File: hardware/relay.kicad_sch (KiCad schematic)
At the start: 5 parts, among them K1 SRD-05VDC-SL-C, Q1 BC847

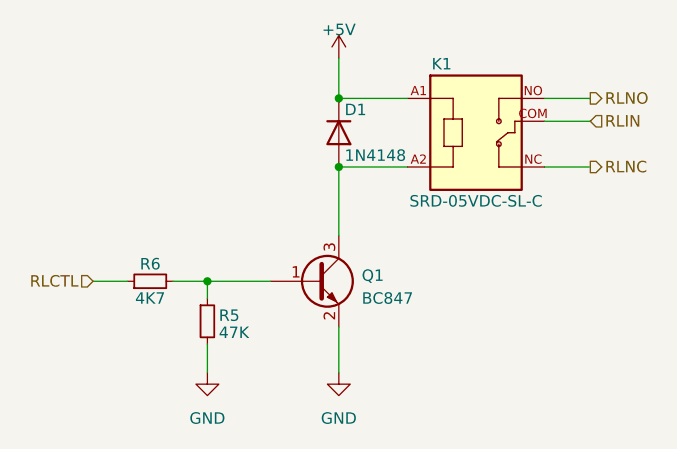
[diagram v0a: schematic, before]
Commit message: * 3V8 Power design fixed * Footprints assigned * Bom exported * PCB filter module placed
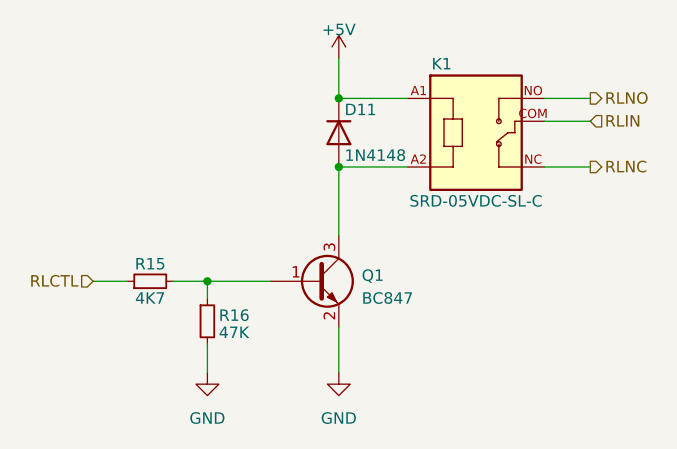
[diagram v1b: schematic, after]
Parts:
- R15: renamed from R6; footprint (none) -> Resistor_SMD:R_0603_1608Metric
- R16: renamed from R5; footprint (none) -> Resistor_SMD:R_0603_1608Metric
- renumbered D1 to D11
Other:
- company: (none) -> Hidro Elektronik
- title: (none) -> 2023 Staj Projesi
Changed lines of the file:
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@@
 (kicad_sch (version 20230121) (generator eeschema)
   (paper "A4")
+  (title_block
+    (title "2023 Staj Projesi")
+    (date "2023-07-24")
+    (rev "1.0")
+    (company "Hidro Elektronik")
+    (comment 1 "Mehmet Emre SAYGI(2019513057@ogr.cu.edu.tr)")
+    (comment 2 "Yilmaz Can DURAN(duranyilmazcan@gmail.com)")
+    (comment 3 "Asli VEZIR(vezirasli@gmail.com)")
+  )
   (junction (at 137.16 88.265) (diameter 0) (color 0 0 0 0)
   )
@@
   (symbol (lib_id "power:GND") (at 137.16 111.125 0) (unit 1)
     (in_bom yes) (on_board yes) (dnp no) (fields_autoplaced)
-    (property "Reference" "#PWR02" (at 137.16 117.475 0)
+    (property "Reference" "#PWR045" (at 137.16 117.475 0)
       (effects (font (size 1.27 1.27)) hide)
     )
@@
       (project "2023-staj-projesi"
         (path "/069db7ad-35cd-4aa8-8111-e026f632a4df/9708c89c-3f17-4bed-9aa3-84d886db37e6"
-          (reference "#PWR02") (unit 1)
+          (reference "#PWR045") (unit 1)
         )
       )
@@
   (symbol (lib_id "Diode:1N4148") (at 137.16 84.455 270) (unit 1)
     (in_bom yes) (on_board yes) (dnp no)
-    (property "Reference" "D1" (at 137.795 81.915 90)
+    (property "Reference" "D11" (at 137.795 81.915 90)
       (effects (font (size 1.27 1.27)) (justify left))
     )
@@
       (project "2023-staj-projesi"
         (path "/069db7ad-35cd-4aa8-8111-e026f632a4df/9708c89c-3f17-4bed-9aa3-84d886db37e6"
-          (reference "D1") (unit 1)
+          (reference "D11") (unit 1)
         )
       )
@@
   (symbol (lib_id "power:+5V") (at 137.16 76.2 0) (unit 1)
     (in_bom yes) (on_board yes) (dnp no) (fields_autoplaced)
-    (property "Reference" "#PWR01" (at 137.16 80.01 0)
+    (property "Reference" "#PWR044" (at 137.16 80.01 0)
       (effects (font (size 1.27 1.27)) hide)
     )
@@
       (project "2023-staj-projesi"
         (path "/069db7ad-35cd-4aa8-8111-e026f632a4df/9708c89c-3f17-4bed-9aa3-84d886db37e6"
-          (reference "#PWR01") (unit 1)
+          (reference "#PWR044") (unit 1)
         )
       )
@@
   (symbol (lib_id "Device:R_Small") (at 116.205 100.965 90) (unit 1)
     (in_bom yes) (on_board yes) (dnp no)
-    (property "Reference" "R6" (at 116.205 99.06 90)
+    (property "Reference" "R15" (at 116.205 99.06 90)
       (effects (font (size 1.27 1.27)))
     )
@@
       (effects (font (size 1.27 1.27)))
     )
-    (property "Footprint" "" (at 116.205 100.965 0)
+    (property "Footprint" "Resistor_SMD:R_0603_1608Metric" (at 116.205 100.965 0)
       (effects (font (size 1.27 1.27)) hide)
     )
@@
       (project "2023-staj-projesi"
         (path "/069db7ad-35cd-4aa8-8111-e026f632a4df/9708c89c-3f17-4bed-9aa3-84d886db37e6"
-          (reference "R6") (unit 1)
+          (reference "R15") (unit 1)
         )
       )
@@
   (symbol (lib_id "Device:R_Small") (at 122.555 105.41 0) (unit 1)
     (in_bom yes) (on_board yes) (dnp no)
-    (property "Reference" "R5" (at 123.825 104.775 0)
+    (property "Reference" "R16" (at 123.825 104.775 0)
       (effects (font (size 1.27 1.27)) (justify left))
     )
@@
       (effects (font (size 1.27 1.27)) (justify left))
     )
-    (property "Footprint" "" (at 122.555 105.41 0)
+    (property "Footprint" "Resistor_SMD:R_0603_1608Metric" (at 122.555 105.41 0)
       (effects (font (size 1.27 1.27)) hide)
     )
@@
       (project "2023-staj-projesi"
         (path "/069db7ad-35cd-4aa8-8111-e026f632a4df/9708c89c-3f17-4bed-9aa3-84d886db37e6"
-          (reference "R5") (unit 1)
+          (reference "R16") (unit 1)
         )
       )
@@
   (symbol (lib_id "power:GND") (at 122.555 111.125 0) (unit 1)
     (in_bom yes) (on_board yes) (dnp no) (fields_autoplaced)
-    (property "Reference" "#PWR03" (at 122.555 117.475 0)
+    (property "Reference" "#PWR043" (at 122.555 117.475 0)
       (effects (font (size 1.27 1.27)) hide)
     )
@@
       (project "2023-staj-projesi"
         (path "/069db7ad-35cd-4aa8-8111-e026f632a4df/9708c89c-3f17-4bed-9aa3-84d886db37e6"
-          (reference "#PWR03") (unit 1)
-        )
-      )
+          (reference "#PWR043") (unit 1)
+        )
+      )
